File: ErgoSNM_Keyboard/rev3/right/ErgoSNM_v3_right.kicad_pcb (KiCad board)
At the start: 2 copper layers, 115.6 x 106.7 mm, 86 parts, among them J1 USB_C_Receptacle_USB2.0, J2 Conn_01x02, J3 Conn_01x08, J4 Conn_01x04, SW1 SW_DPDT_x2, SW2 RESET, U1 TPS61220DCK, U2 E73-2G4M08S1C, Y1 32.768kHz

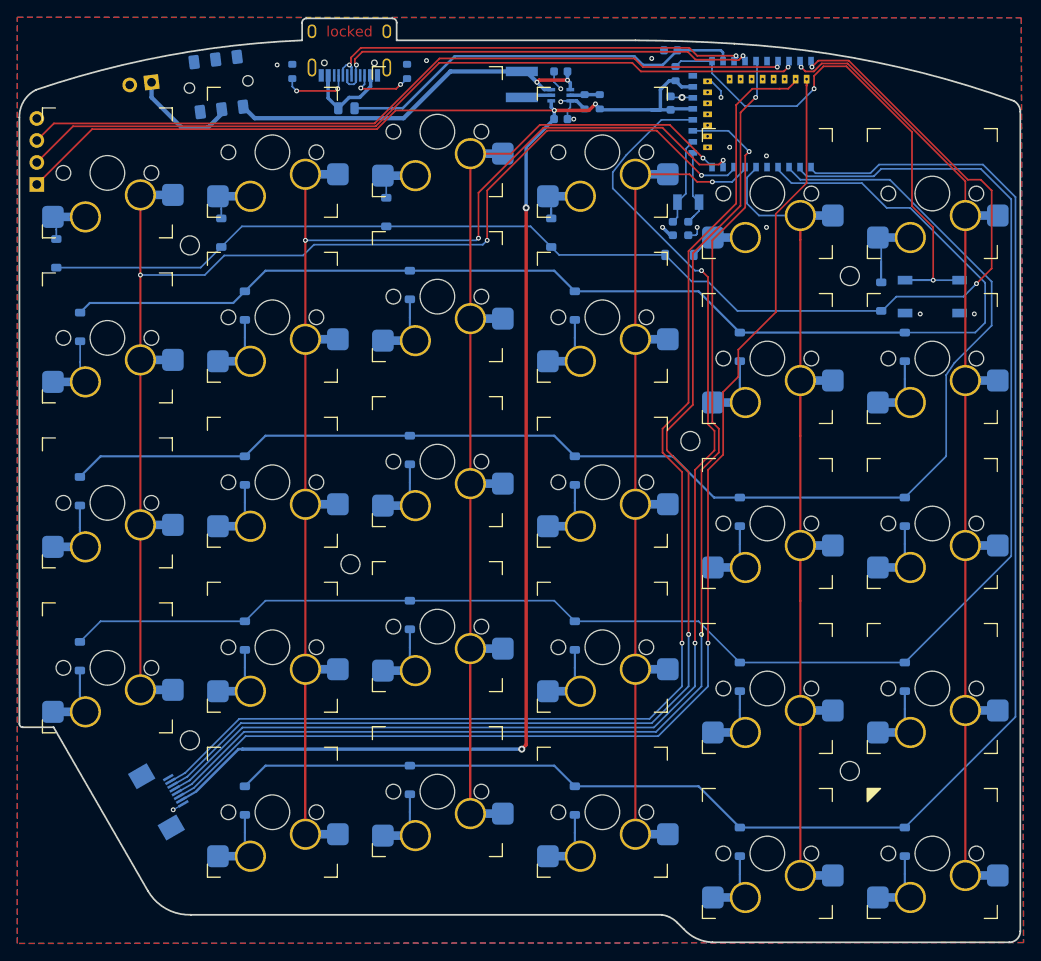
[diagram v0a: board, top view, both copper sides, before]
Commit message: Add LDO for USB
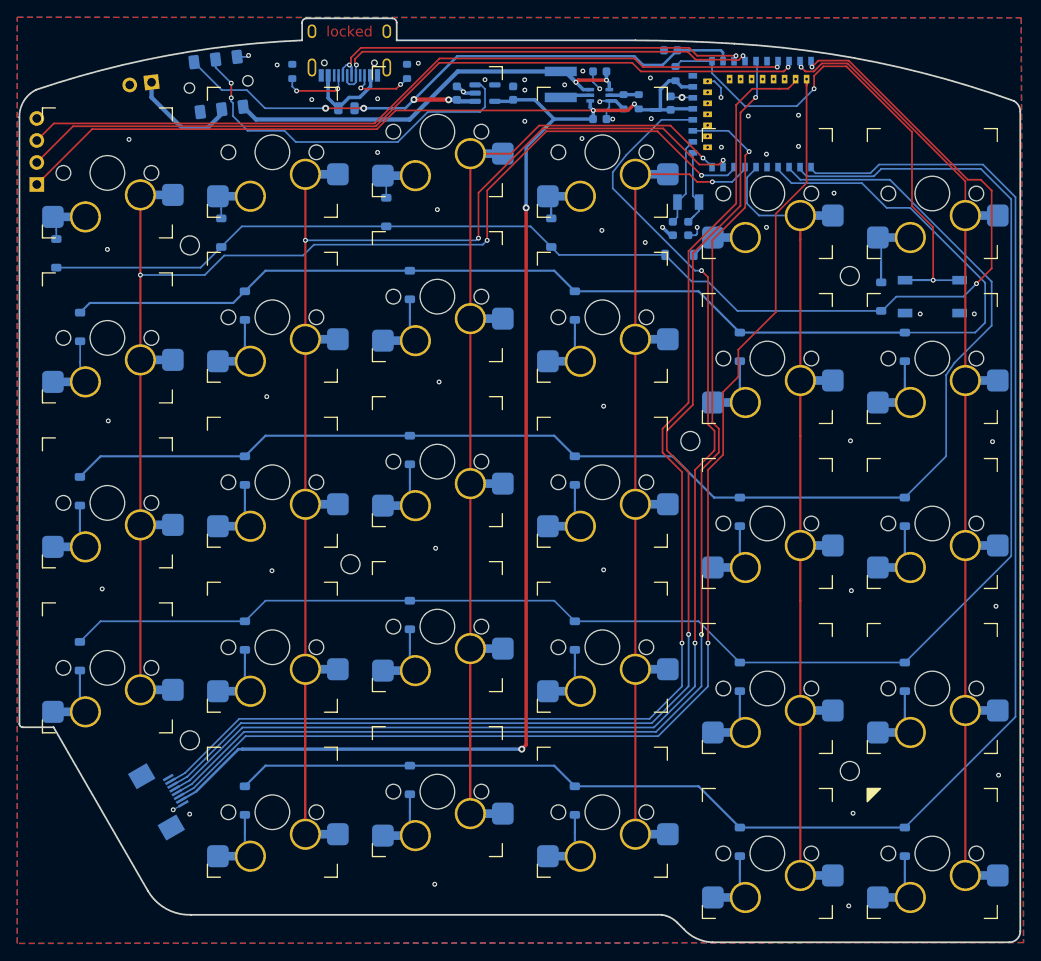
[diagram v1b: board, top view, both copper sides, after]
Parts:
- added C7: 1uF, Capacitor_SMD:C_0603_1608Metric, B.Cu at (125.1, 42.4)
- added C8: 1uF, Capacitor_SMD:C_0603_1608Metric, B.Cu at (131.6, 42.4)
- added U3: RT9013-33GB, Package_TO_SOT_SMD:SOT-23-5, B.Cu at (128.4, 42.4)
- R1: value 560k -> 1.2M
- R4: value 200k -> 220k
- moved C1 4.50 mm to (141.6, 45.4)
- moved C2 4.50 mm to (141.6, 39.9)
- moved L1 4.50 mm to (137.1, 41.4)
- moved R1 4.50 mm to (146.1, 43.4)
- moved R4 4.50 mm to (144.4, 43.4)
- moved U1 4.50 mm to (141.6, 42.6)
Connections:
- SW1 pad 4: (no net) -> +5V
- SW1 pad 5: (no net) -> Net-(SW1B-B)
- SW1 pad 6: (no net) -> GND
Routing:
- net Net-(SW1B-B): track 0.00 -> 42.8 mm, vias 0 -> 2
- net +5V: track 47.7 -> 76.2 mm, vias 0 -> 4
- net VDD: track 206.0 -> 218.3 mm
- net +BATT: track 45.6 -> 50.2 mm
- net GND: track 17.9 -> 22.0 mm, vias 16 -> 55
